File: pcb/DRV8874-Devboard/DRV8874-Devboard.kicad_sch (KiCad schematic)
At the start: 40 parts, among them J1 Conn_01x04_Pin, J2 Screw_Terminal_01x02, J3 Conn_01x03_Pin, J4 Conn_01x03_Pin, J5 Conn_01x04_Pin, J6 Conn_01x03_Pin, J7 Conn_01x03_Pin, J8 Conn_01x04_Pin, J9 Conn_01x03_Pin, U1 DRV8874, U2 BL9342, U4 SN65HVD230, U5 TPS16630PWPR, U7 TinyThinker_J1

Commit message: Started working on layout
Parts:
- added C6: 330uF, Capacitor_SMD:CP_Elec_10x10.5, symbol Device:C_Polarized
- added C7: 22nF, Capacitor_SMD:C_0603_1608Metric, symbol Device:C
- added C8, C9: 100nF, Capacitor_SMD:C_0402_1005Metric, symbol Device:C
- added J10: Conn_01x06_Pin, Connector_PinHeader_2.54mm:PinHeader_1x06_P2.54mm_Vertical, symbol Connector:Conn_01x06_Pin
- added J11: Conn_01x04_Pin, Connector_PinHeader_2.54mm:PinHeader_1x04_P2.54mm_Vertical, symbol Connector:Conn_01x04_Pin
- added J12: Conn_01x03_Pin, Connector_PinHeader_2.54mm:PinHeader_1x03_P2.54mm_Vertical, symbol Connector:Conn_01x03_Pin
- added R16: 15k, Resistor_SMD:R_0603_1608Metric, symbol Device:R
- added R17: 75k, Resistor_SMD:R_0603_1608Metric, symbol Device:R
- added R18: 20k, Resistor_SMD:R_0603_1608Metric, symbol Device:R
- added R19: 2k2, Resistor_SMD:R_0402_1005Metric, symbol Device:R
- added R20: 10k, Resistor_SMD:R_0805_2012Metric, symbol Device:R
- added U3: DRV8874, Package_SO:HTSSOP-16-1EP_4.4x5mm_P0.65mm_EP3.4x5mm_Mask2.46x2.31mm, symbol Custom_Library:DRV8874
- J1, J3, J4, J5, J6, J7, J8, J9: now fitted
- R10, R7: footprint PCM_JLCPCB:R_0603 -> Resistor_SMD:R_0603_1608Metric
- U1: footprint Package_SO:HTSSOP-16-1EP_4.4x5mm_P0.65mm_EP3.4x5mm_Mask2.66x2.46mm -> Package_SO:HTSSOP-16-1EP_4.4x5mm_P0.65mm_EP3.4x5mm_Mask2.46x2.31mm
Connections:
- net +3.3V: now also U7.13 (+3.3V), U7.16 (+3.3V), U7.25 (+3.3V), U7.28 (+3.3V), U7.37 (+3.3V), J10.6 (Pin_6), J11.1 (Pin_1), R16.1, R20.1, U3.3 (nSLEEP)
- net +5V: now also U7.1 (+5V_EXT)
- net +BATT_PROT: now also C12.1, U2.5 (VIN), C6.1, C8.1, C9.1, U3.11 (VM)
- net GND: now also U7.10 (GND), U7.11 (GND), U7.14 (GND), U7.15 (GND), U7.18 (GND), U7.19 (GND), U7.2 (GND), U7.22 (GND), U7.23 (GND), U7.26 (GND), U7.27 (GND), U7.30 (GND), U7.31 (GND), U7.34 (GND), U7.35 (GND), U7.38 (GND), U7.39 (GND), U7.4 (GND), U7.6 (GND), U7.7 (GND), C6.2, C8.2, J10.1 (Pin_1), J11.3 (Pin_3), J12.3 (Pin_3), R17.2, R18.2, R19.2, U3.15 (GND), U3.17 (PAD), U3.9 (PGND)
- net Phase_A+: no longer U1.8 (OUT1)
- net Phase_A-: no longer U1.10 (OUT2)
- net CAN_RS: now reaches J6.2 (Pin_2), U4.8 (Rs)
- net CAN_RS_R: now reaches J6.3 (Pin_3), R2.1
- net A_IN1: now reaches U1.1 (EN/IN1)
- net A_VCP: now reaches C2.2, U1.12 (VCP)
- net A_CPH: now reaches C1.1, U1.13 (CPH)
- net A_CPL: now reaches C1.2, U1.14 (CPL)
- net A_IN2: now reaches U1.2 (PH/IN2)
- net A_nFault: now reaches R4.2, U1.4 (nFAULT)
- net A_VREF: now reaches R13.2, R14.1, U1.5 (VREF)
- net A_IPROPI: now reaches R1.1, U1.6 (IPROPI)
- net A_IPROPI: now also U7.17 (ADC1_IN9)
- net A_IMODE: now reaches J9.2 (Pin_2), U1.7 (IMODE)
- net BL_FB: now reaches C13.1, R11.2, R12.2, U2.3 (FB)
- net CAN_TERM: now reaches J4.2 (Pin_2), R3.1
- net TPS_MON: now reaches R7.1, U5.14 (IMON)
- net TPS_FLT: now reaches R6.2, U5.15 (*FLT)
- net B_IPROPI: now reaches U7.21 (ADC1_IN15)
- net TPS_OVP: now reaches R10.1, R9.2, U5.8 (OVP)
- net BL_BST: now reaches C11.1, U2.1 (BST)
- net BL_SW: now reaches C11.2, D2.1 (K), L2.1, U2.6 (SW)
- net TPS_DVDT: now reaches C4.1, U5.10 (DVDT)
- net A_IMODE_R: now reaches J9.1 (Pin_1), R15.1
- net TPS_UVLO: now reaches R8.2, R9.1, U5.7 (UVLO)
- net TPS_ILIM: now reaches R5.1, U5.11 (ILIM)
- net SPI1_NSS: now reaches U7.51 (SPI1_NSS)
- net SPI1_NSS: now also J10.5 (Pin_5)
- net SPI1_SCK: now reaches U7.53 (SPI1_SCK)
- net SPI1_SCK: now also J10.4 (Pin_4)
- net SPI1_MISO: now reaches U7.55 (SPI1_MISO)
- net SPI1_MISO: now also J10.3 (Pin_3)
- net SPI1_MOSI: now reaches U7.57 (SPI1_MOSI)
- net SPI1_MOSI: now also J10.2 (Pin_2)
- net BL9342_EN renamed BL_EN
- net PMODE_A renamed A_PMODE
- new net A_OUT+: U1.8 (OUT1)
- new net A_OUT-: U1.10 (OUT2)
- new net B_CPH: C7.1, U3.13 (CPH)
- new net B_CPL: C7.2, U3.14 (CPL)
- new net B_IMODE: J12.2 (Pin_2), U3.7 (IMODE)
- new net B_IMODE_R: J12.1 (Pin_1), R18.1
- new net B_IN1: U3.1 (EN/IN1)
- new net B_IN2: U3.2 (PH/IN2)
- new net B_IRPOPI: R19.1, U3.6 (IPROPI)
- new net B_OUT+: U3.8 (OUT1)
- new net B_OUT-: U3.10 (OUT2)
- new net B_PMODE: J11.2 (Pin_2), U3.16 (PMODE)
- new net B_VCP: C9.2, U3.12 (VCP)
- new net B_VREF: R16.2, R17.1, U3.5 (VREF)
- new net B_nFault: R20.2, U3.4 (nFAULT)
- no-connect marks 6 -> 29
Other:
- note added: "Battery Connector"
- note added: "Boot Switch + RST"
- note added: "PHASE B"
- note added: "SPI Connector"
- note added: "Tiny Thinker Pinout"
- note added: "USB"
- moved on the sheet: C10, C11, C12, C13, C4, D2, J2, L2, R10, R11, R12, R2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

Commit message: checkpoint
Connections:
- net Phase_A+ is gone; now on net A_OUT+: J1.4 (Pin_4)
- net Phase_A- is gone; now on net A_OUT-: J1.2 (Pin_2)
- net Phase_B+ is gone; now on net B_OUT+: J1.3 (Pin_3)
- net Phase_B- is gone; now on net B_OUT-: J1.1 (Pin_1)
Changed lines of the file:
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@@
 		)
 	)
-	(label "Phase_B+"
+	(label "B_OUT+"
 		(at 313.69 143.51 180)
 		(effects
@@
 		)
 	)
-	(label "Phase_A-"
+	(label "A_OUT-"
 		(at 313.69 146.05 180)
 		(effects
@@
 		)
 	)
-	(label "Phase_A+"
+	(label "A_OUT+"
 		(at 313.69 140.97 180)
 		(effects
@@
 		)
 	)
-	(label "Phase_B-"
+	(label "B_OUT-"
 		(at 313.69 148.59 180)
 		(effects

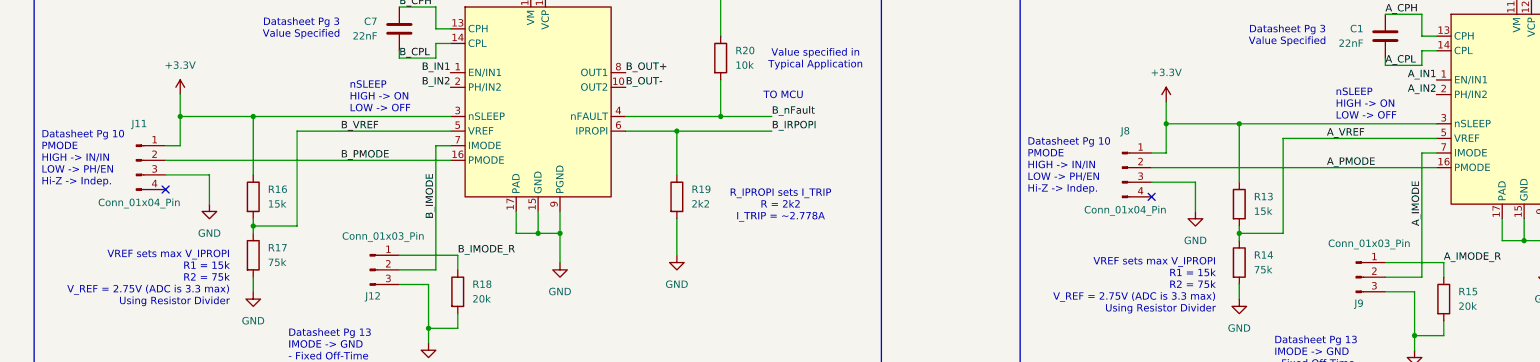
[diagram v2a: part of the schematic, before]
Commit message: removed jumper to switch PMODE since IN/I N seems to have the most benefits
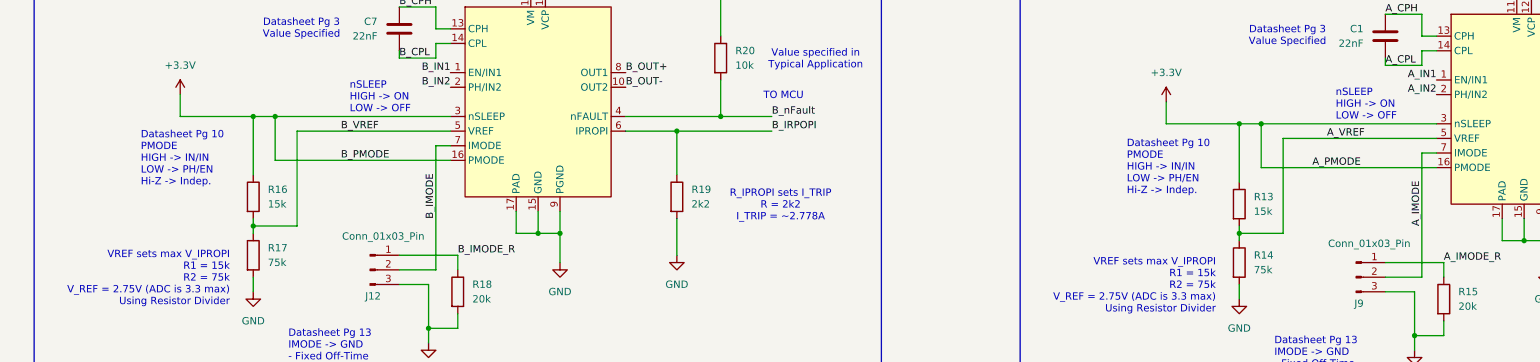
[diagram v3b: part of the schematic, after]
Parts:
- removed J11, J8: Conn_01x04_Pin, Connector_PinHeader_2.54mm:PinHeader_1x04_P2.54mm_Vertical, symbol Connector:Conn_01x04_Pin
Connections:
- net A_PMODE is gone; now on net +3.3V: U1.16 (PMODE)
- net B_PMODE is gone; now on net +3.3V: U3.16 (PMODE)
- no-connect marks 29 -> 27

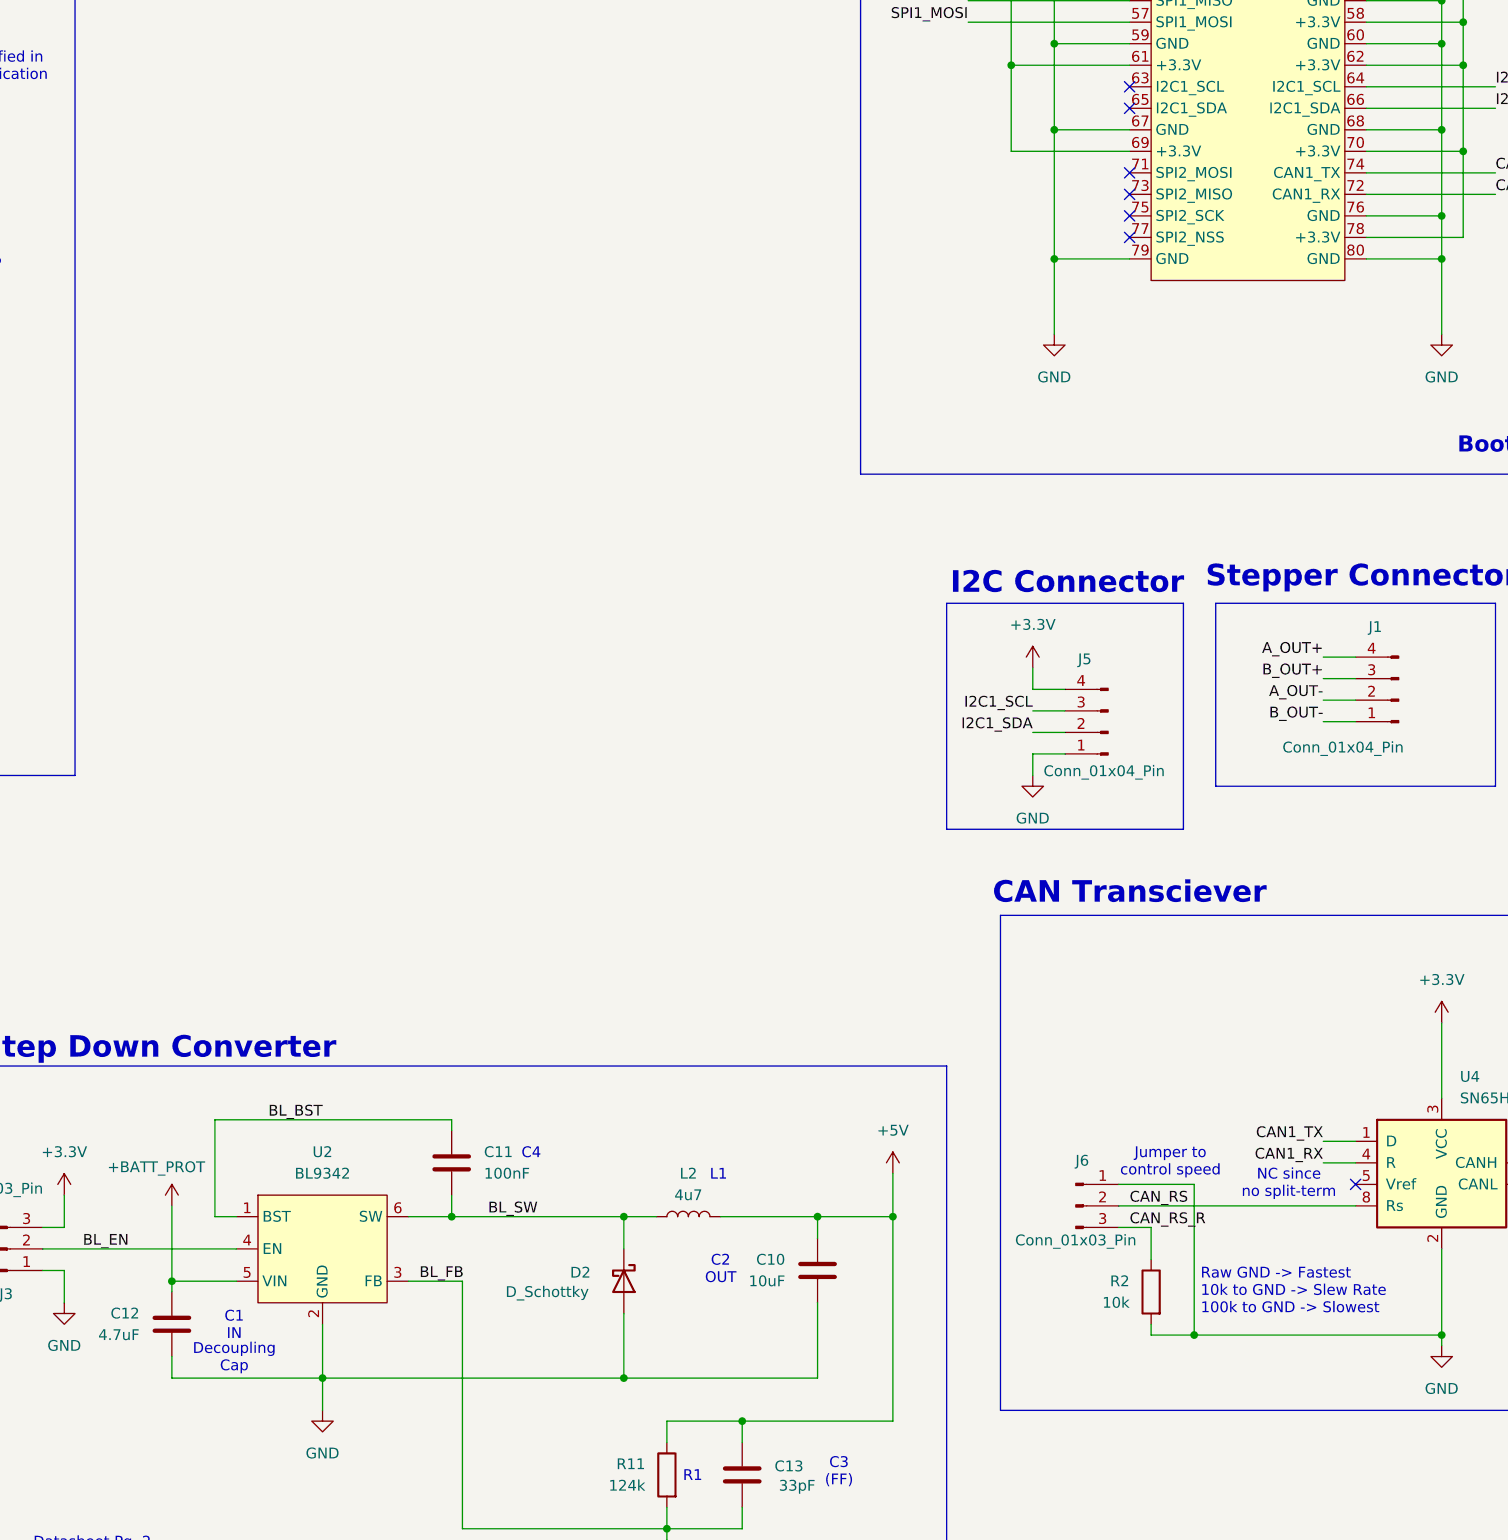
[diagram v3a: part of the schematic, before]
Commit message: Routed and laid out BL9342 step down
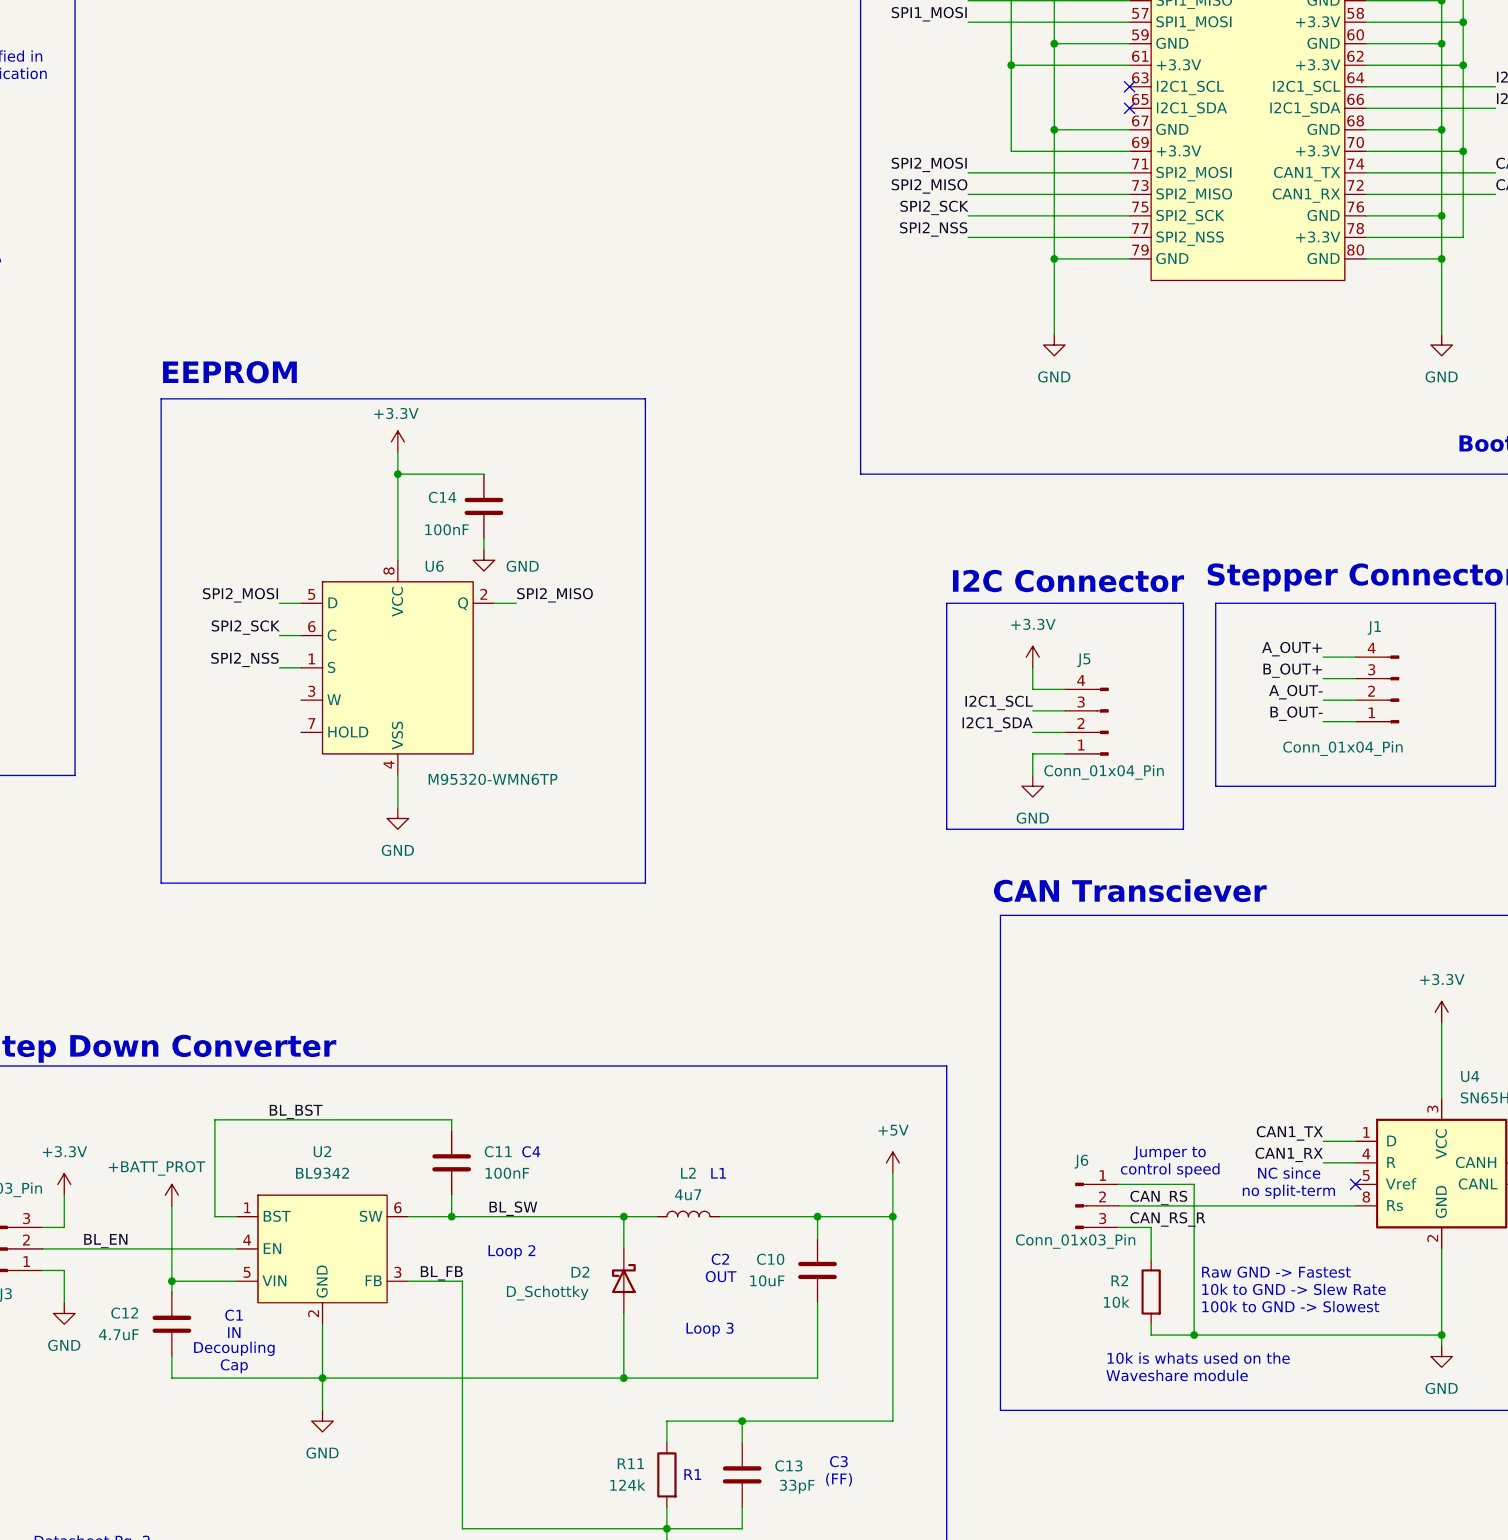
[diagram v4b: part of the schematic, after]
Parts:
- added C14: 100nF, Capacitor_SMD:C_0402_1005Metric, symbol Device:C
- added U6: M95320-WMN6TP, Package_SO:SO-8_3.9x4.9mm_P1.27mm, symbol Custom_Library:M95320-WMN6TP
- C1, C7: footprint Capacitor_SMD:C_0603_1608Metric -> Capacitor_SMD:C_0402_1005Metric; JLCPCB Part # C21122 -> C1532
- R2, R20, R4, R6: footprint Resistor_SMD:R_0805_2012Metric -> Resistor_SMD:R_0402_1005Metric; JLCPCB Part # C17414 -> C25744
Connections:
- net +3.3V: now also C14.1, U6.8 (VCC)
- net GND: now also C14.2, U6.4 (VSS)
- net SPI2_MOSI: now reaches U7.71 (SPI2_MOSI)
- net SPI2_MOSI: now also U6.5 (D)
- net SPI2_MISO: now reaches U7.73 (SPI2_MISO)
- net SPI2_MISO: now also U6.2 (Q)
- net SPI2_SCK: now reaches U7.75 (SPI2_SCK)
- net SPI2_SCK: now also U6.6 (C)
- net SPI2_NSS: now reaches U7.77 (SPI2_NSS)
- net SPI2_NSS: now also U6.1 (S)
- no-connect marks 27 -> 23
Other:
- note added: "10k is whats used on the Waveshare module"
- note added: "EEPROM"
- note added: "Loop 2"
- note added: "Loop 3"

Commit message: generated CSV to see pricing
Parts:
- C3, C6: FT Rotation Offset (none) -> 180; JLCPCB Part # C3032175 -> C46550419
- J1, J10, J12, J3, J4, J5, J6, J7, J9, U7: now not fitted
- J2: JLCPCB Part # (none) -> C430601
- U1, U3: JLCPCB Part # (none) -> C1855818
- U2: JLCPCB Part # (none) -> C93176
- U4: JLCPCB Part # (none) -> C12084
- U5: JLCPCB Part # (none) -> C1849461
- U6: FT Rotation Offset (none) -> -90; JLCPCB Part # (none) -> C283459

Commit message: updated rotation offsets
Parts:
- U2: FT Rotation Offset (none) -> 90
- U5: footprint HTSSOP20_PWP_TEX -> Package_SO:HTSSOP-20-1EP_4.4x6.5mm_P0.65mm_EP2.85x4mm; FT Rotation Offset (none) -> 90

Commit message: removed DNP checks
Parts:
- J1, J10, J12, J3, J4, J5, J6, J7, J9, U7: now fitted
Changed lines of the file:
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@@
 		(in_bom yes)
 		(on_board yes)
-		(dnp yes)
+		(dnp no)
 		(property "Reference" "J5"
 			(at 284.734 141.224 0)
@@
 		(in_bom yes)
 		(on_board yes)
-		(dnp yes)
+		(dnp no)
 		(property "Reference" "J6"
 			(at 285.242 200.406 0)
@@
 		(in_bom yes)
 		(on_board yes)
-		(dnp yes)
+		(dnp no)
 		(property "Reference" "J7"
 			(at 398.018 209.804 0)
@@
 		(in_bom yes)
 		(on_board yes)
-		(dnp yes)
+		(dnp no)
 		(fields_autoplaced yes)
 		(property "Reference" "U7"
@@
 		(in_bom yes)
 		(on_board yes)
-		(dnp yes)
+		(dnp no)
 		(property "Reference" "J12"
 			(at -93.472 111.252 0)
@@
 		(in_bom yes)
 		(on_board yes)
-		(dnp yes)
+		(dnp no)
 		(property "Reference" "J4"
 			(at 362.204 207.264 0)
@@
 		(in_bom yes)
 		(on_board yes)
-		(dnp yes)
+		(dnp no)
 		(property "Reference" "J3"
 			(at 158.242 216.154 0)
@@
 		(in_bom yes)
 		(on_board yes)
-		(dnp yes)
+		(dnp no)
 		(property "Reference" "J9"
 			(at 77.978 112.522 0)
@@
 		(in_bom yes)
 		(on_board yes)
-		(dnp yes)
+		(dnp no)
 		(property "Reference" "J10"
 			(at 361.188 141.986 0)
@@
 		(in_bom yes)
 		(on_board yes)
-		(dnp yes)
+		(dnp no)
 		(fields_autoplaced yes)
 		(property "Reference" "U7"
@@
 		(in_bom yes)
 		(on_board yes)
-		(dnp yes)
+		(dnp no)
 		(property "Reference" "J1"
 			(at 319.024 137.414 0)
